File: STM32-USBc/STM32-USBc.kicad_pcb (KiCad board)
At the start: 2 copper layers, 28 parts, among them J1 Conn_01x04_Pin, J2 Conn_01x04_Pin, J3 Conn_01x04_Pin, P1 USB_C_Plug_USB2.0, SW1 SW_SPDT, U1 STM32F103C8T6, U2 AMS1117-3.3, Y3 16MHz

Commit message: pre rooting
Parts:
- moved R2 80.0 mm to (183.0, 78.5)
- moved C7 74.0 mm to (192.0, 79.8)
- moved C11 72.2 mm to (192.0, 94.0)
- moved R4 65.4 mm to (192.0, 97.5), turned to 180 degrees
- moved R5 63.4 mm to (195.0, 97.5)
- moved J2 62.4 mm to (192.8, 74.0), turned to -90 degrees
- moved SW1 59.1 mm to (177.5, 76.0), turned to -90 degrees
- moved J3 51.1 mm to (190.0, 100.5), turned to 90 degrees
- moved D1 50.0 mm to (215.5, 97.7), turned to -90 degrees
- moved U2 49.0 mm to (206.8, 98.2), turned to -90 degrees
- moved C1 48.0 mm to (206.8, 92.7)
- moved C2 42.7 mm to (211.8, 97.7), turned to 90 degrees
- moved R1 42.6 mm to (215.5, 95.0), turned to 90 degrees
- moved J1 4.50 mm to (205.0, 74.0)
- turned C10 to 180 degrees
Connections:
- C10 pad 1: Net-(C10-Pad1) -> +3.3V
- FB1 pad 2: Net-(C10-Pad1) -> +3.3V

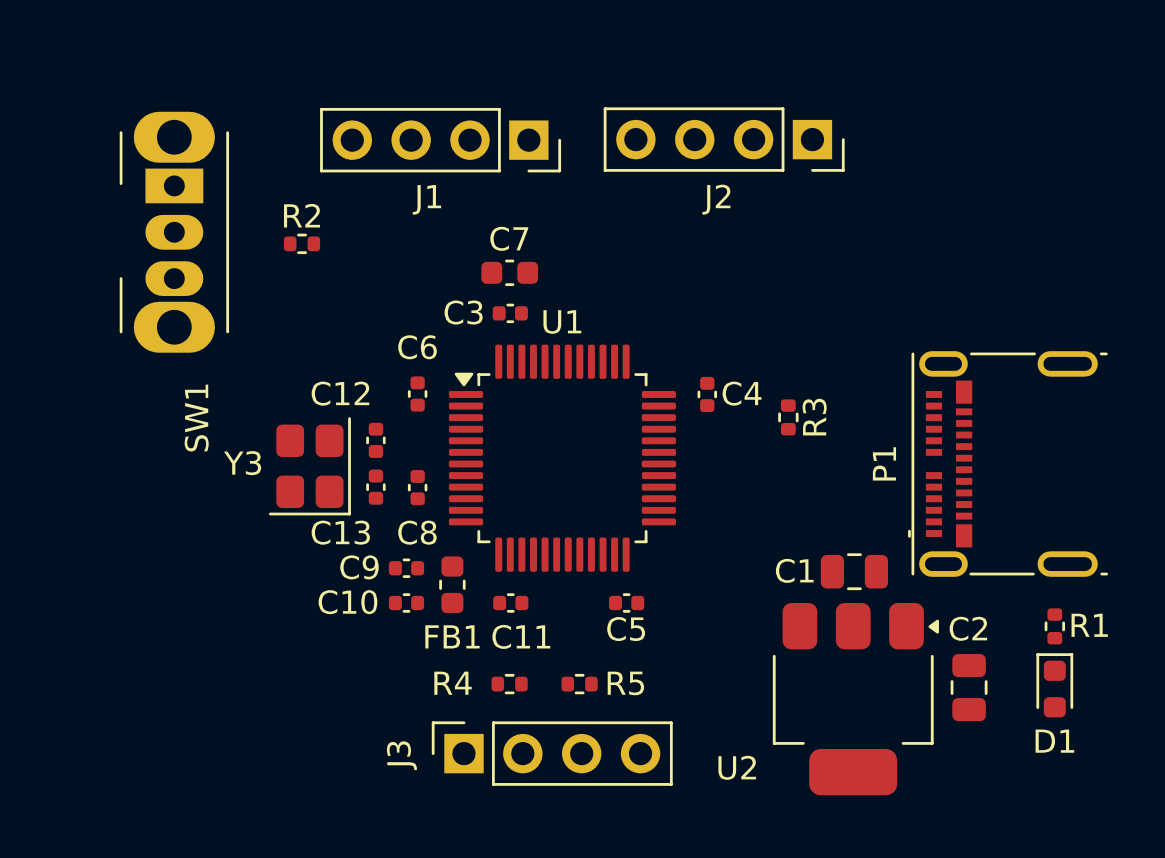
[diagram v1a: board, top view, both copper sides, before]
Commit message: 3d model of switch + layout borders
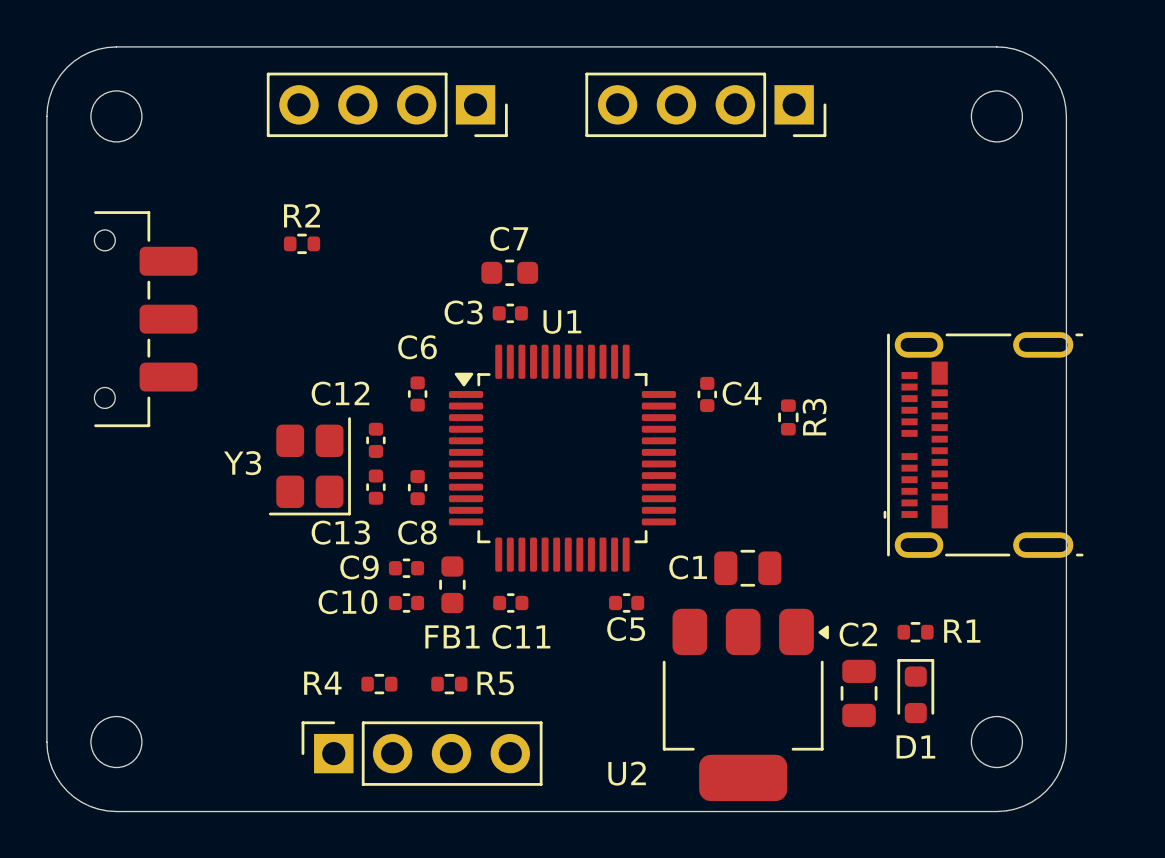
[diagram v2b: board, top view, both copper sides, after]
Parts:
- added H1: MountingHole, MountingHole:MountingHole_2.2mm_M2, F.Cu at (175.0, 73.0)
- added H2: MountingHole, MountingHole:MountingHole_2.2mm_M2, F.Cu at (175.0, 100.0)
- added H3: MountingHole, MountingHole:MountingHole_2.2mm_M2, F.Cu at (213.0, 73.0)
- added H4: MountingHole, MountingHole:MountingHole_2.2mm_M2, F.Cu at (213.0, 100.0)
- SW1: footprint Button_Switch_THT:SW_Slide_SPDT_Angled_CK_OS102011MA1Q -> Button_Switch_SMD:SW_SPDT_CK_JS102011SAQN
- moved SW1 6.49 mm to (174.5, 81.8)
- moved R1 6.02 mm to (209.5, 95.3), turned to 180 degrees
- moved D1 6.01 mm to (209.5, 98.0)
- moved J3 5.62 mm to (184.4, 100.5)
- moved R4 5.62 mm to (186.3, 97.5)
- moved R5 5.62 mm to (189.4, 97.5)
- moved C2 4.76 mm to (207.1, 97.9)
- moved U2 4.76 mm to (202.1, 98.4)
- moved C1 4.60 mm to (202.2, 92.5)
- moved J2 2.76 mm to (190.5, 72.5)
- moved J1 1.70 mm to (204.2, 72.5)
- moved P1 1.34 mm to (212.4, 87.2)
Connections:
- C10 pad 1: +3.3V -> Net-(C10-Pad1)
- FB1 pad 2: +3.3V -> Net-(C10-Pad1)
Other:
- board outline added: 44 x 33 mm

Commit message: switch to usb b
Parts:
- removed P1: USB_C_Plug_USB2.0, Connector_USB:USB_C_Receptacle_Molex_105450-0101
- added J4: USB_B_Micro, Connector_USB:USB_Micro-B_Wuerth_629105150521, F.Cu at (212.1, 86.6)
- moved C12 0.98 mm to (186.2, 86.0)
- moved C13 0.98 mm to (186.2, 88.0)
- moved Y3 0.98 mm to (183.3, 87.1), turned to -90 degrees
- moved C7 0.56 mm to (191.7, 80.2)
- moved C4 0.48 mm to (200.2, 85.4)
- moved C6 0.40 mm to (188.2, 84.7)
- moved C3 0.37 mm to (191.7, 81.8)
- moved C5 0.37 mm to (196.8, 93.8)
- moved C8 0.27 mm to (188.2, 88.9)
- moved U1 0.16 mm to (194.2, 87.9)
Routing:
- net GND: track 0.00 -> 9.34 mm
- net +3.3V: track 0.00 -> 9.27 mm
- net /HSE_IN: track 0.00 -> 8.55 mm
- net /HSE_OUT: track 0.00 -> 6.35 mm
- net +3.3VA: track 0.00 -> 1.93 mm
- added copper zone on B.Cu, net GND

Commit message: final rooting and texts
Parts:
- moved D1 3.95 mm to (212.5, 95.4)
- moved R1 3.61 mm to (212.4, 93.1), turned to 0 degrees
- moved R2 3.03 mm to (181.8, 81.3), turned to 90 degrees
- moved C2 2.75 mm to (207.2, 95.2)
- moved C1 1.80 mm to (203.2, 91.0)
- moved U2 1.80 mm to (202.1, 96.6)
- moved C5 0.35 mm to (197.0, 94.0)
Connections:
- C10 pad 1: Net-(C10-Pad1) -> +3.3V
- FB1 pad 2: Net-(C10-Pad1) -> +3.3V
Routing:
- net +3.3V: track 9.27 -> 165.0 mm, vias 0 -> 6
- net /BOOT0: track 0.00 -> 21.9 mm
- net /USART1_TX: track 0.00 -> 20.6 mm
- net /USART1_RX: track 0.00 -> 20.1 mm
- net GND: track 9.34 -> 28.5 mm, vias 0 -> 20
- net /SWDIO: track 0.00 -> 16.6 mm
- net /I2C2_SCL: track 0.00 -> 16.5 mm
- net /I2C2_SDA: track 0.00 -> 12.6 mm
- net /SWCLK: track 0.00 -> 12.1 mm
- net /USB_D+: track 0.00 -> 11.8 mm
- net /USB_D-: track 0.00 -> 11.8 mm
- net /NRST: track 0.00 -> 10.9 mm
- net +3.3VA: track 1.93 -> 6.68 mm
- net /SW_BOOT0: track 0.00 -> 4.51 mm
- net /PWR_LED_K: track 0.00 -> 1.75 mm
- added copper zone on F.Cu, net +3.3V
- added copper zone on F.Cu, net GND
- added copper zone on F.Cu, net VBUS
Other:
- board text added: "BOOT"
- board text added: "EXPERIMENTAL raptor is comming :)"
- board text added: "ON"
- board text added: "SWD"
- board text added: "UART"
- board text added: "USB"
